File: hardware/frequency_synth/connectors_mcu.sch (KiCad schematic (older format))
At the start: 8 parts, among them P1001 CONN_01X02, P1002 CONN_01X02, U1001 boosterpack_ti, U1002 CONN_SMA_2GND

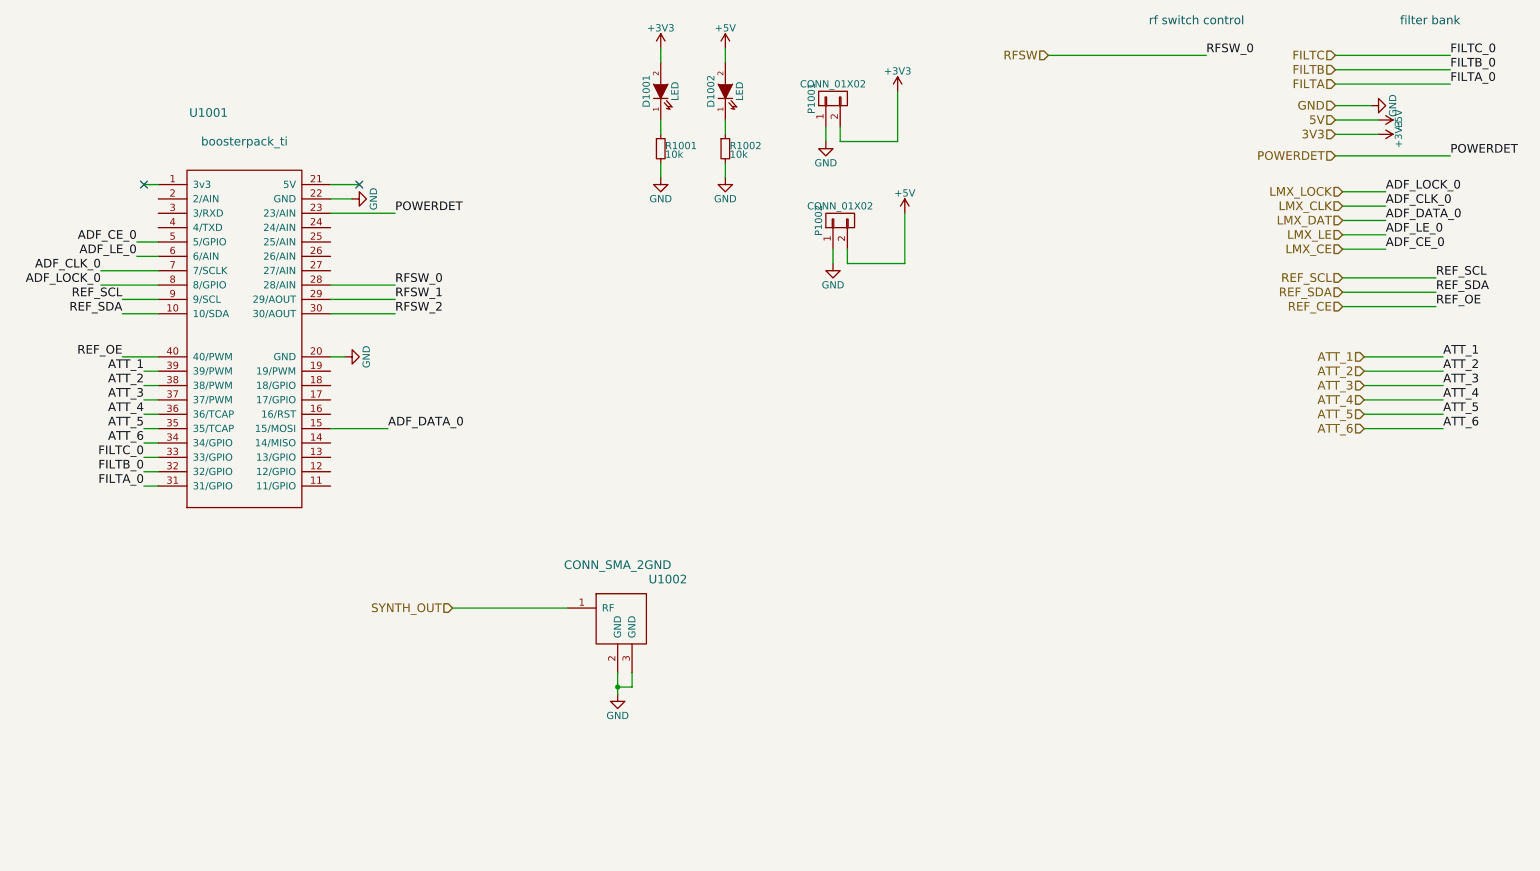
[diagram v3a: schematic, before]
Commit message: synth - initial component placement layout on everybody but lmx2592
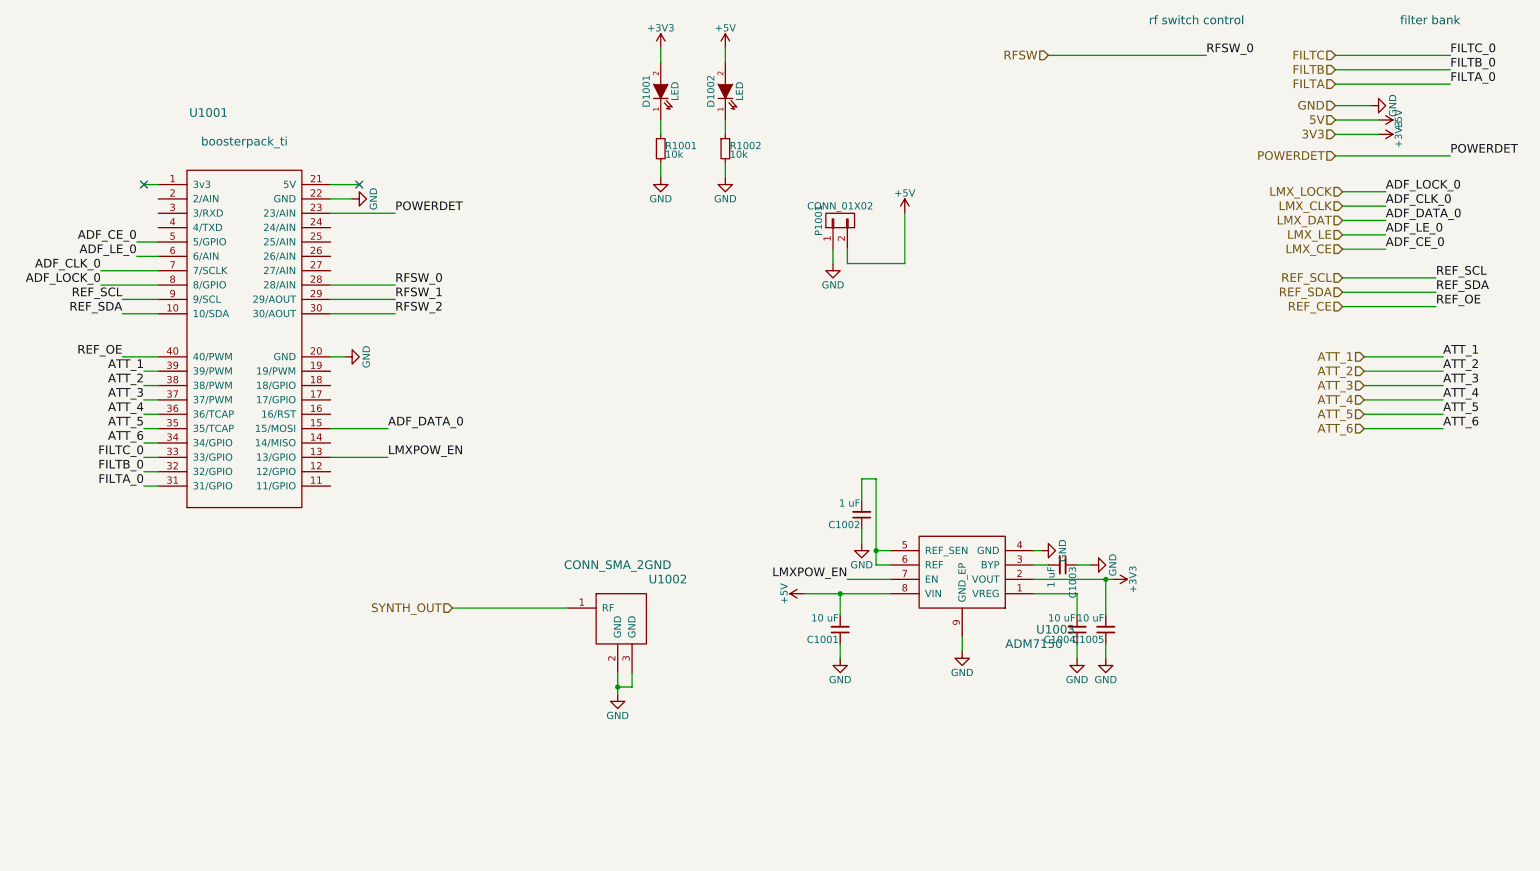
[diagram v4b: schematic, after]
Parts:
- removed P1001: CONN_01X02, Terminal_Blocks:TerminalBlock_Pheonix_PT-3.5mm_2pol, symbol CONN_01X02
- added C1001, C1004, C1005: 10 uF, Capacitors_SMD:C_0603, symbol C_Small
- added C1002, C1003: 1 uF, Capacitors_SMD:C_0402, symbol C_Small
- added U1003: ADM7150, Housings_DFN_QFN:DFN-8-1EP_3x3mm_Pitch0.5mm, symbol ADM7150
- renumbered P1002 to P1001
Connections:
- net +3V3: now also C1005.2, U1003.2 (VOUT)
- net +5V: now also C1001.2, U1003.8 (VIN)
- net GND: now also C1001.1, C1002.1, C1003.1, C1004.1, C1005.1, U1003.4 (GND), U1003.9 (GND_EP)
- net LMXPOW_EN: now reaches U1001.13 (13/GPIO)
- net LMXPOW_EN: now also U1003.7 (EN)
- new net: C1004.2, U1003.1 (VREG)
- new net: C1003.2, U1003.3 (BYP)
- new net: C1002.2, U1003.5 (REF_SEN), U1003.6 (REF)

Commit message: finished initial component placement
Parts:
- added R?: PTC/MF-NSMF110-2, symbol R
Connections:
- net +5V: now also R?.2; no longer P1001.2 (P2)
- new net: P1001.2 (P2), R?.1
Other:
- moved on the sheet: P1001
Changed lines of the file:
@@
 L CONN_01X02 P1001
 U 1 1 573282FD
-P 6100 2000
-F 0 "P1001" H 6100 2150 50  0000 C CNN
-F 1 "CONN_01X02" V 6200 2000 50  0000 C CNN
-F 2 "Terminal_Blocks:TerminalBlock_Pheonix_PT-3.5mm_2pol" H 6100 2000 50  0001 C CNN
-F 3 "" H 6100 2000 50  0000 C CNN
-	1    6100 2000
+P 6100 1950
+F 0 "P1001" H 6100 2100 50  0000 C CNN
+F 1 "CONN_01X02" V 6200 1950 50  0000 C CNN
+F 2 "Terminal_Blocks:TerminalBlock_Pheonix_PT-3.5mm_2pol" H 6100 1950 50  0001 C CNN
+F 3 "" H 6100 1950 50  0000 C CNN
+	1    6100 1950
 	0    -1   -1   0
 $EndComp
@@
 L GND #PWR0208
 U 1 1 57328303
-P 6050 2300
-F 0 "#PWR0208" H 6050 2050 50  0001 C CNN
-F 1 "GND" H 6050 2150 50  0000 C CNN
-F 2 "" H 6050 2300 50  0000 C CNN
-F 3 "" H 6050 2300 50  0000 C CNN
-	1    6050 2300
-	1    0    0    -1
-$EndComp
-Wire Wire Line
-	6550 1950 6550 2300
-Wire Wire Line
-	6550 2300 6150 2300
-Wire Wire Line
-	6150 2300 6150 2200
-Wire Wire Line
-	6050 2200 6050 2300
+P 6050 2800
+F 0 "#PWR0208" H 6050 2550 50  0001 C CNN
+F 1 "GND" H 6050 2650 50  0000 C CNN
+F 2 "" H 6050 2800 50  0000 C CNN
+F 3 "" H 6050 2800 50  0000 C CNN
+	1    6050 2800
+	1    0    0    -1
+$EndComp
+Wire Wire Line
+	6550 1950 6550 2800
+Wire Wire Line
+	6550 2800 6150 2800
+Wire Wire Line
+	6150 2800 6150 2550
+Wire Wire Line
+	6050 2150 6050 2800
 $Comp
 L +5V #PWR0209
@@
 L +5V #PWR0213
 U 1 1 572C8470
-P 5850 4600
-F 0 "#PWR0213" H 5850 4450 50  0001 C CNN
-F 1 "+5V" H 5850 4740 50  0000 C CNN
-F 2 "" H 5850 4600 50  0000 C CNN
-F 3 "" H 5850 4600 50  0000 C CNN
-	1    5850 4600
+P 5650 4600
+F 0 "#PWR0213" H 5650 4450 50  0001 C CNN
+F 1 "+5V" H 5650 4740 50  0000 C CNN
+F 2 "" H 5650 4600 50  0000 C CNN
+F 3 "" H 5650 4600 50  0000 C CNN
+	1    5650 4600
 	0    -1   -1   0
 $EndComp
@@
 Wire Wire Line
 	2950 3650 2550 3650
-Wire Wire Line
-	5850 4600 6450 4600
 $Comp
 L C_Small C1001
@@
 	7950 4750 7950 4500
 Connection ~ 7950 4500
+$Comp
+L R R?
+U 1 1 572DA9D7
+P 6150 2400
+F 0 "R?" V 6230 2400 50  0000 C CNN
+F 1 "PTC/MF-NSMF110-2" V 6350 2500 50  0000 C CNN
+F 2 "" V 6080 2400 50  0000 C CNN
+F 3 "" H 6150 2400 50  0000 C CNN
+	1    6150 2400
+	1    0    0    -1
+$EndComp
+Wire Wire Line
+	6150 2150 6150 2250
+Wire Wire Line
+	5650 4600 6450 4600
 $EndSCHEMATC

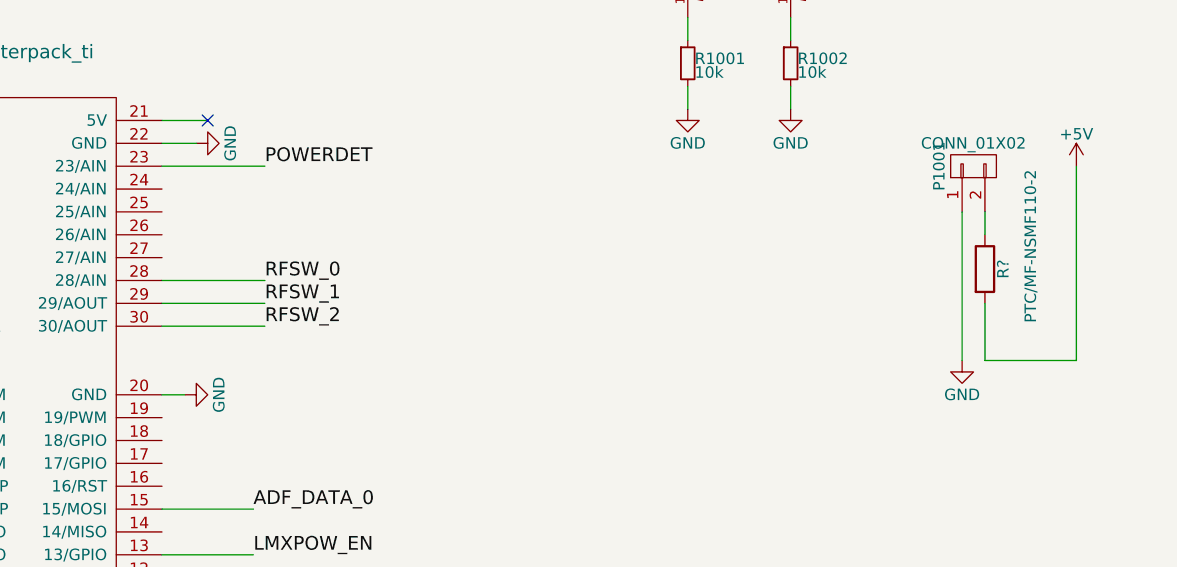
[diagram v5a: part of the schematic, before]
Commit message: added sma edge launch cutout SLOT cal board
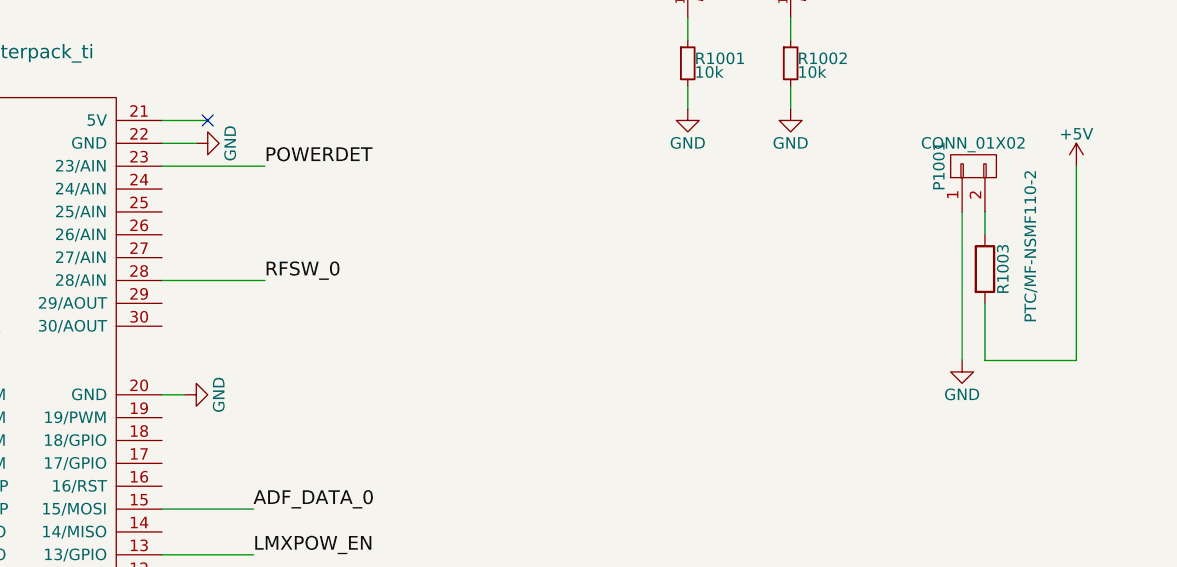
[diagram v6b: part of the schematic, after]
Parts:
- R1003: renamed from R?; footprint (none) -> Resistors_SMD:R_1206
- U1001: footprint vna_footprints:ti_booster40 -> Connect:IDC_Header_Straight_40pins
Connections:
- net RFSW_1: no longer names the net of U1001.29 (29/AOUT)
- net RFSW_2: no longer names the net of U1001.30 (30/AOUT)
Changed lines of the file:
@@
 F 0 "U1001" H 1700 4450 60  0000 C CNN
 F 1 "boosterpack_ti" H 1950 4250 60  0000 C CNN
-F 2 "vna_footprints:ti_booster40" H 1700 4450 60  0001 C CNN
+F 2 "Connect:IDC_Header_Straight_40pins" H 1700 4450 60  0001 C CNN
 F 3 "" H 1700 4450 60  0000 C CNN
 	1    1950 2850
@@
 Text Label 950  2450 2    60   ~ 0
 ADF_LOCK_0
-Text Label 3000 2650 0    60   ~ 0
-RFSW_2
-Text Label 3000 2550 0    60   ~ 0
-RFSW_1
 Text Label 3000 2450 0    60   ~ 0
 RFSW_0
@@
 Text HLabel 3400 4700 0    60   Input ~ 0
 SYNTH_OUT
-Wire Wire Line
-	4650 5150 4650 5250
-Connection ~ 4550 5250
-Wire Wire Line
-	4550 5150 4550 5300
-Wire Wire Line
-	3400 4700 4200 4700
-Wire Wire Line
-	2550 1950 3000 1950
-Wire Wire Line
-	2650 2950 2550 2950
-Wire Wire Line
-	950  2450 1350 2450
-Wire Wire Line
-	1200 2250 1350 2250
-Wire Wire Line
-	1200 2150 1350 2150
-Wire Wire Line
-	950  2350 1350 2350
-Wire Wire Line
-	5300 1700 5300 1600
-Wire Wire Line
-	5300 1300 5300 1400
-Wire Wire Line
-	5300 800  5300 900
-Wire Wire Line
-	2550 2650 3000 2650
-Wire Wire Line
-	2550 2550 3000 2550
-Wire Wire Line
-	3000 2450 2550 2450
-Wire Wire Line
-	1250 3350 1350 3350
-Wire Wire Line
-	1250 3450 1350 3450
-Wire Wire Line
-	1250 3850 1350 3850
-Wire Wire Line
-	1250 3750 1350 3750
-Wire Wire Line
-	1250 3650 1350 3650
-Wire Wire Line
-	1250 3550 1350 3550
-Wire Wire Line
-	9600 1800 9900 1800
-Wire Wire Line
-	9600 1900 9900 1900
-Wire Wire Line
-	9600 2000 9900 2000
-Wire Wire Line
-	9600 2100 9900 2100
-Wire Wire Line
-	9600 2200 9900 2200
-Wire Wire Line
-	9550 1200 9800 1200
-Wire Wire Line
-	9550 850  10350 850
-Wire Wire Line
-	9550 950  10350 950
-Wire Wire Line
-	9550 1050 10350 1050
-Wire Wire Line
-	7550 850  8650 850
-Wire Wire Line
-	1250 1750 1350 1750
-Wire Wire Line
-	2750 1750 2550 1750
-Wire Wire Line
-	2550 1850 2700 1850
 Text HLabel 7550 850  0    60   Input ~ 0
 RFSW
@@
 Text HLabel 9550 1300 0    60   Input ~ 0
 5V
-Wire Wire Line
-	9850 1300 9550 1300
 Text Label 10350 1550 0    60   ~ 0
 POWERDET
 Text HLabel 9550 1550 0    60   Input ~ 0
 POWERDET
-Wire Wire Line
-	10350 1550 9550 1550
 Text HLabel 9600 1800 0    60   Input ~ 0
 LMX_LOCK
@@
 Text Label 1100 2950 2    60   ~ 0
 REF_OE
-Wire Wire Line
-	1100 2650 1350 2650
-Wire Wire Line
-	1100 2550 1350 2550
-Wire Wire Line
-	1100 2950 1350 2950
-Wire Wire Line
-	2550 3450 2950 3450
 Text Label 10250 2400 0    60   ~ 0
 REF_SCL
@@
 Text HLabel 9600 2600 0    60   Input ~ 0
 REF_CE
-Wire Wire Line
-	10250 2400 9600 2400
-Wire Wire Line
-	9600 2500 10250 2500
-Wire Wire Line
-	10250 2600 9600 2600
 Text HLabel 9550 1400 0    60   Input ~ 0
 3V3
@@
 	0    1    1    0
 $EndComp
-Wire Wire Line
-	9850 1400 9550 1400
-Wire Wire Line
-	1350 3050 1250 3050
-Wire Wire Line
-	1350 3150 1250 3150
-Wire Wire Line
-	1350 3250 1250 3250
 Text Label 1250 3050 2    60   ~ 0
 ATT_1
@@
 Text HLabel 9750 3350 0    60   Input ~ 0
 ATT_5
-Wire Wire Line
-	10300 2950 9750 2950
-Wire Wire Line
-	9750 3050 10300 3050
-Wire Wire Line
-	10300 3150 9750 3150
-Wire Wire Line
-	9750 3250 10300 3250
-Wire Wire Line
-	10300 3350 9750 3350
 Text HLabel 9750 3450 0    60   Input ~ 0
 ATT_6
-Wire Wire Line
-	9750 3450 10300 3450
 NoConn ~ 2750 1750
 NoConn ~ 1250 1750
@@
 	1    0    0    -1
 $EndComp
-Wire Wire Line
-	6550 1950 6550 2800
-Wire Wire Line
-	6550 2800 6150 2800
-Wire Wire Line
-	6150 2800 6150 2550
-Wire Wire Line
-	6050 2150 6050 2800
 $Comp
 L +5V #PWR0209
@@
 	-1   0    0    -1
 $EndComp
-Wire Wire Line
-	4650 5250 4550 5250
 $Comp
 L +5V #PWR0210
@@
 	1    0    0    -1
 $EndComp
-Wire Wire Line
-	4850 1700 4850 1600
-Wire Wire Line
-	4850 1300 4850 1400
-Wire Wire Line
-	4850 800  4850 900
 $Comp
 L +3V3 #PWR0212
@@
 	1    0    0    -1
 $EndComp
-Wire Wire Line
-	6950 4900 6950 5000
 $Comp
 L C_Small C1003
@@
 	0    -1   -1   0
 $EndComp
-Wire Wire Line
-	7850 4400 7750 4400
-Wire Wire Line
-	7450 4400 7550 4400
 $Comp
 L GND #PWR0217
@@
 	0    -1   -1   0
 $EndComp
-Wire Wire Line
-	7500 4300 7450 4300
 $Comp
 L C_Small C1002
@@
 	-1   0    0    1
 $EndComp
-Wire Wire Line
-	6350 4400 6450 4400
-Wire Wire Line
-	6350 3800 6350 4400
-Wire Wire Line
-	6350 4300 6450 4300
 $Comp
 L GND #PWR0218
@@
 	1    0    0    -1
 $EndComp
-Wire Wire Line
-	6250 4250 6250 4150
-Wire Wire Line
-	6250 3950 6250 3800
-Wire Wire Line
-	6250 3800 6350 3800
-Connection ~ 6350 4300
-Wire Wire Line
-	6450 4500 6150 4500
 Text Label 6150 4500 2    60   ~ 0
 LMXPOW_EN
 Text Label 2950 3650 0    60   ~ 0
 LMXPOW_EN
-Wire Wire Line
-	2950 3650 2550 3650
 $Comp
 L C_Small C1001
@@
 	1    0    0    -1
 $EndComp
-Wire Wire Line
-	6100 5050 6100 4950
-Wire Wire Line
-	6100 4750 6100 4600
-Connection ~ 6100 4600
 $Comp
 L C_Small C1004
@@
 	1    0    0    -1
 $EndComp
-Wire Wire Line
-	7750 5050 7750 4950
-Wire Wire Line
-	7450 4600 7750 4600
-Wire Wire Line
-	7750 4600 7750 4750
-Wire Wire Line
-	7450 4500 8000 4500
 $Comp
 L C_Small C1005
@@
 	1    0    0    -1
 $EndComp
+$Comp
+L R R1003
+U 1 1 572DA9D7
+P 6150 2400
+F 0 "R1003" V 6230 2400 50  0000 C CNN
+F 1 "PTC/MF-NSMF110-2" V 6350 2500 50  0000 C CNN
+F 2 "Resistors_SMD:R_1206" V 6080 2400 50  0001 C CNN
+F 3 "" H 6150 2400 50  0000 C CNN
+	1    6150 2400
+	1    0    0    -1
+$EndComp
+Wire Wire Line
+	4650 5150 4650 5250
+Connection ~ 4550 5250
+Wire Wire Line
+	4550 5150 4550 5300
+Wire Wire Line
+	3400 4700 4200 4700
+Wire Wire Line
+	2550 1950 3000 1950
+Wire Wire Line
+	2650 2950 2550 2950
+Wire Wire Line
+	950  2450 1350 2450
+Wire Wire Line
+	1200 2250 1350 2250
+Wire Wire Line
+	1200 2150 1350 2150
+Wire Wire Line
+	950  2350 1350 2350
+Wire Wire Line
+	5300 1700 5300 1600
+Wire Wire Line
+	5300 1300 5300 1400
+Wire Wire Line
+	5300 800  5300 900
+Wire Wire Line
+	3000 2450 2550 2450
+Wire Wire Line
+	1250 3350 1350 3350
+Wire Wire Line
+	1250 3450 1350 3450
+Wire Wire Line
+	1250 3850 1350 3850
+Wire Wire Line
+	1250 3750 1350 3750
+Wire Wire Line
+	1250 3650 1350 3650
+Wire Wire Line
+	1250 3550 1350 3550
+Wire Wire Line
+	9600 1800 9900 1800
+Wire Wire Line
+	9600 1900 9900 1900
+Wire Wire Line
+	9600 2000 9900 2000
+Wire Wire Line
+	9600 2100 9900 2100
+Wire Wire Line
+	9600 2200 9900 2200
+Wire Wire Line
+	9550 1200 9800 1200
+Wire Wire Line
+	9550 850  10350 850
+Wire Wire Line
+	9550 950  10350 950
+Wire Wire Line
+	9550 1050 10350 1050
+Wire Wire Line
+	7550 850  8650 850
+Wire Wire Line
+	1250 1750 1350 1750
+Wire Wire Line
+	2750 1750 2550 1750
+Wire Wire Line
+	2550 1850 2700 1850
+Wire Wire Line
+	9850 1300 9550 1300
+Wire Wire Line
+	10350 1550 9550 1550
+Wire Wire Line
+	1100 2650 1350 2650
+Wire Wire Line
+	1100 2550 1350 2550
+Wire Wire Line
+	1100 2950 1350 2950
+Wire Wire Line
+	2550 3450 2950 3450
+Wire Wire Line
+	10250 2400 9600 2400
+Wire Wire Line
+	9600 2500 10250 2500
+Wire Wire Line
+	10250 2600 9600 2600
+Wire Wire Line
+	9850 1400 9550 1400
+Wire Wire Line
+	1350 3050 1250 3050
+Wire Wire Line
+	1350 3150 1250 3150
+Wire Wire Line
+	1350 3250 1250 3250
+Wire Wire Line
+	10300 2950 9750 2950
+Wire Wire Line
+	9750 3050 10300 3050
+Wire Wire Line
+	10300 3150 9750 3150
+Wire Wire Line
+	9750 3250 10300 3250
+Wire Wire Line
+	10300 3350 9750 3350
+Wire Wire Line
+	9750 3450 10300 3450
+Wire Wire Line
+	6550 1950 6550 2800
+Wire Wire Line
+	6550 2800 6150 2800
+Wire Wire Line
+	6150 2800 6150 2550
+Wire Wire Line
+	6050 2150 6050 2800
+Wire Wire Line
+	4650 5250 4550 5250
+Wire Wire Line
+	4850 1700 4850 1600
+Wire Wire Line
+	4850 1300 4850 1400
+Wire Wire Line
+	4850 800  4850 900
+Wire Wire Line
+	6950 4900 6950 5000
+Wire Wire Line
+	7850 4400 7750 4400
+Wire Wire Line
+	7450 4400 7550 4400
+Wire Wire Line
+	7500 4300 7450 4300
+Wire Wire Line
+	6350 4400 6450 4400
+Wire Wire Line
+	6350 3800 6350 4400
+Wire Wire Line
+	6350 4300 6450 4300
+Wire Wire Line
+	6250 4250 6250 4150
+Wire Wire Line
+	6250 3950 6250 3800
+Wire Wire Line
+	6250 3800 6350 3800
+Connection ~ 6350 4300
+Wire Wire Line
+	6450 4500 6150 4500
+Wire Wire Line
+	2950 3650 2550 3650
+Wire Wire Line
+	6100 5050 6100 4950
+Wire Wire Line
+	6100 4750 6100 4600
+Connection ~ 6100 4600
+Wire Wire Line
+	7750 5050 7750 4950
+Wire Wire Line
+	7450 4600 7750 4600
+Wire Wire Line
+	7750 4600 7750 4750
+Wire Wire Line
+	7450 4500 8000 4500
 Wire Wire Line
 	7950 5050 7950 4950
@@
 	7950 4750 7950 4500
 Connection ~ 7950 4500
-$Comp
-L R R?
-U 1 1 572DA9D7
-P 6150 2400
-F 0 "R?" V 6230 2400 50  0000 C CNN
-F 1 "PTC/MF-NSMF110-2" V 6350 2500 50  0000 C CNN
-F 2 "" V 6080 2400 50  0000 C CNN
-F 3 "" H 6150 2400 50  0000 C CNN
-	1    6150 2400
-	1    0    0    -1
-$EndComp
 Wire Wire Line
 	6150 2150 6150 2250

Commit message: work on synth layout - removed filter bank inverters
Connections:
- net ~FILTA: now reaches U1001.17 (17/GPIO)
- net ~FILTB: now reaches U1001.18 (18/GPIO)
- net ~FILTC: now reaches U1001.19 (19/PWM)
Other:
- moved on the sheet: C1001, C1002, C1003, C1004, C1005, U1002, U1003
